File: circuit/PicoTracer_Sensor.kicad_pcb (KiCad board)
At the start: 2 copper layers, 150 x 46 mm, 19 parts, among them J8 Conn_01x08_Socket, U1 LBR-127HLD, U10 LBR-127HLD, U11 LBR-127HLD, U12 LBR-127HLD, U13 LBR-127HLD, U14 LBR-127HLD

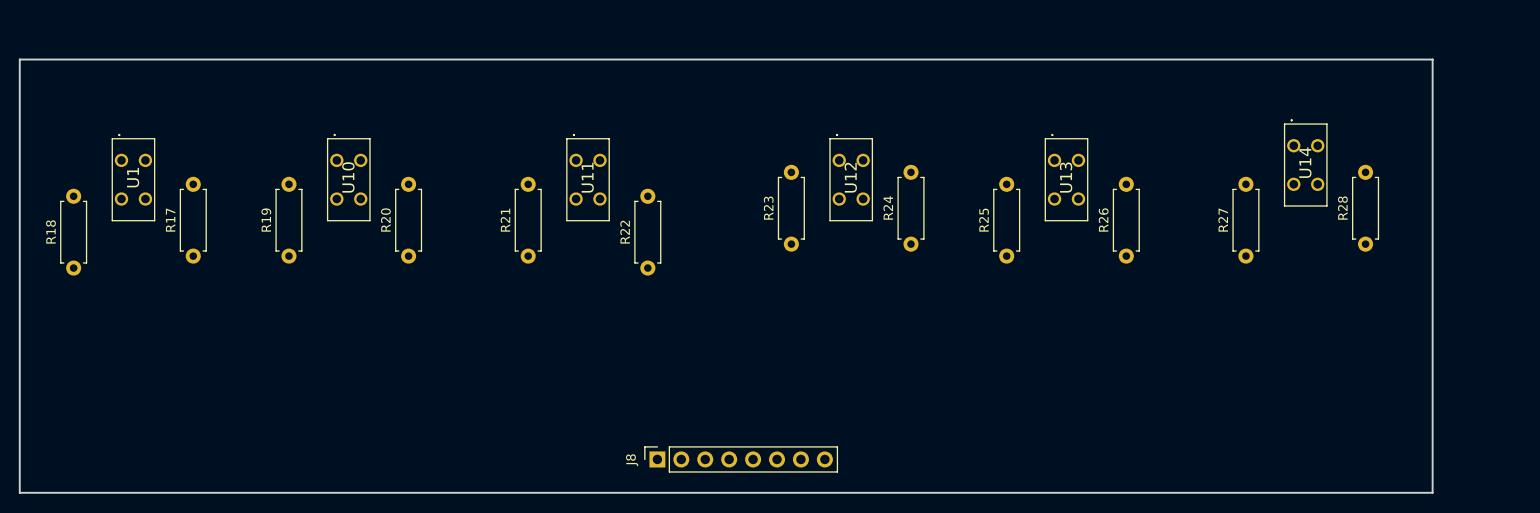
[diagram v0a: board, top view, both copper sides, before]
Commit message: 配線図：配線まで完了　ガーバーファイル出すときに水色の線を出さないよう注意！
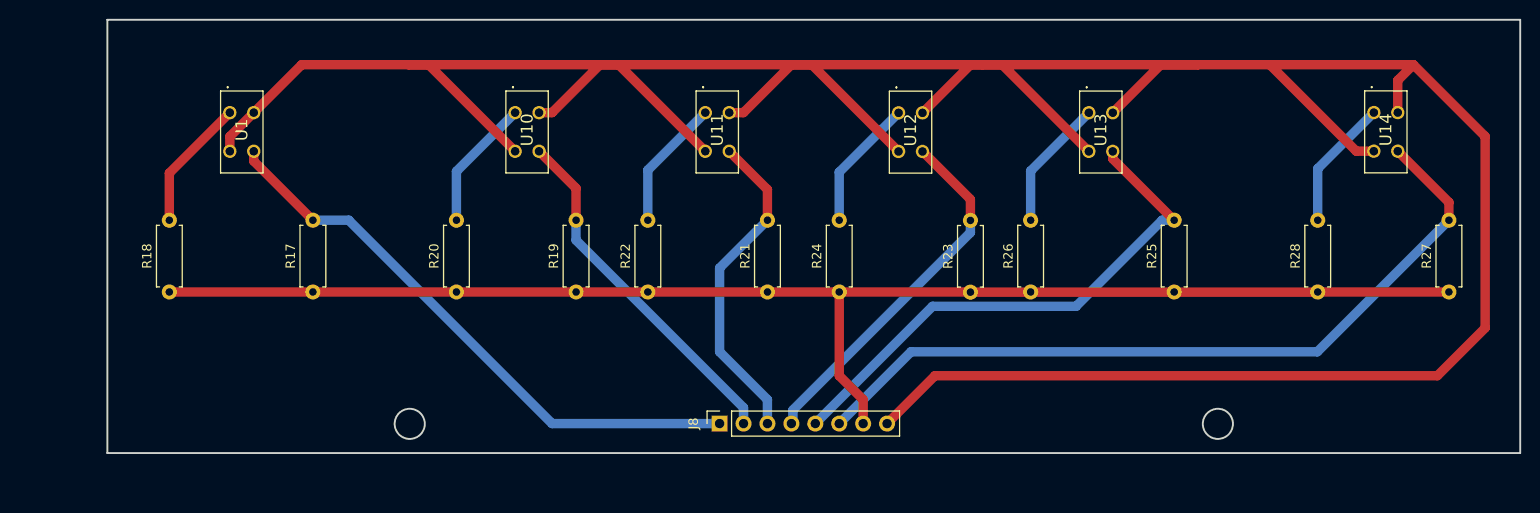
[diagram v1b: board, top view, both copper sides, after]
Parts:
- moved R19 30.7 mm to (121.9, 100.3)
- moved R21 25.7 mm to (142.2, 100.3)
- moved R27 21.9 mm to (214.6, 100.3)
- moved R23 19.7 mm to (163.8, 100.3)
- moved U10 19.6 mm to (115.5, 81.3)
- moved R25 18.2 mm to (185.4, 100.3)
- moved U11 14.6 mm to (135.6, 81.3)
- moved R17 13.3 mm to (94.0, 100.3)
- moved U1 12.6 mm to (85.2, 81.3)
- moved R26 10.9 mm to (170.2, 100.3)
- moved R18 10.5 mm to (78.7, 100.3)
- moved U14 9.20 mm to (206.6, 81.3)
- moved R24 9.16 mm to (149.9, 100.3)
- moved U12 8.07 mm to (156.2, 81.3)
- moved J8 7.62 mm to (137.2, 114.3)
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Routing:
- net Net-(J8-Pin_8): track 0.00 -> 347.1 mm
- net Net-(J8-Pin_7): track 0.00 -> 150.9 mm
- net Net-(J8-Pin_6): track 0.00 -> 83.3 mm
- net Net-(J8-Pin_1): track 0.00 -> 62.0 mm
- net Net-(J8-Pin_5): track 0.00 -> 57.1 mm
- net Net-(J8-Pin_4): track 0.00 -> 38.9 mm
- net Net-(J8-Pin_2): track 0.00 -> 37.9 mm
- net Net-(J8-Pin_3): track 0.00 -> 34.8 mm
- net Net-(U1-ANODE(LONG)): track 0.00 -> 14.1 mm
- net Net-(U12-ANODE(LONG)): track 0.00 -> 14.0 mm
- net Net-(U10-ANODE(LONG)): track 0.00 -> 14.0 mm
- net Net-(U13-ANODE(LONG)): track 0.00 -> 14.0 mm
- net Net-(U11-ANODE(LONG)): track 0.00 -> 13.9 mm
- net Net-(U14-ANODE(LONG)): track 0.00 -> 13.9 mm
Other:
- outline, holes or cut-outs redrawn

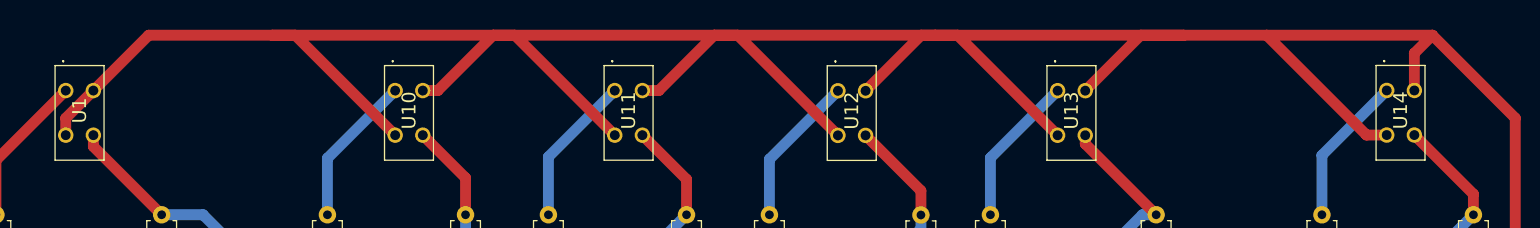
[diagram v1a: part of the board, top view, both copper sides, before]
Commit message: PicoTracer-backupsファイルを管理外に変更　センサー、メイン配線図ファイル修正、その他ファイル更新
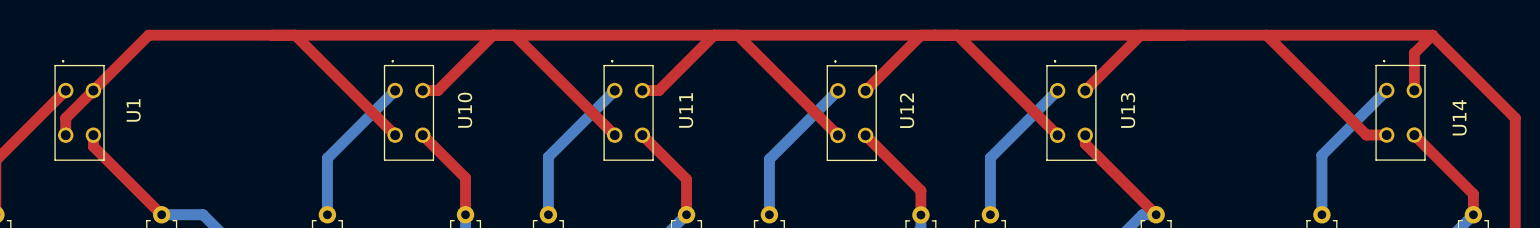
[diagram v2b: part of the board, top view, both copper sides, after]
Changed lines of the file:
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@@
 			(drillshape 0)
 			(scaleselection 1)
-			(outputdirectory "./")
+			(outputdirectory "PicoTracer_Sensor_Garber/")
 		)
 	)
@@
 		(tags "Undefined or Miscellaneous")
 		(property "Reference" "U13"
-			(at -1.825 1.27 90)
+			(at -1.825 6.52 90)
 			(layer "F.SilkS")
 			(effects
@@
 		)
 		(fp_text user "${REFERENCE}"
-			(at -1.825 1.27 90)
+			(at -1.825 6.52 90)
 			(layer "F.Fab")
 			(effects
@@
 		(tags "Undefined or Miscellaneous")
 		(property "Reference" "U10"
-			(at -1.825 1.27 90)
+			(at -1.825 6.47 90)
 			(layer "F.SilkS")
 			(effects
@@
 		)
 		(fp_text user "${REFERENCE}"
-			(at -1.825 1.27 90)
+			(at -1.825 6.47 90)
 			(layer "F.Fab")
 			(effects
@@
 		(tags "Undefined or Miscellaneous")
 		(property "Reference" "U11"
-			(at -1.825 1.27 90)
+			(at -1.825 6.6 90)
 			(layer "F.SilkS")
 			(effects
@@
 		)
 		(fp_text user "${REFERENCE}"
-			(at -1.825 1.27 90)
+			(at -1.825 6.6 90)
 			(layer "F.Fab")
 			(effects
@@
 		(tags "Undefined or Miscellaneous")
 		(property "Reference" "U12"
-			(at -1.825 1.27 90)
+			(at -1.825 6.4 90)
 			(layer "F.SilkS")
 			(effects
@@
 		)
 		(fp_text user "${REFERENCE}"
-			(at -1.825 1.27 90)
+			(at -1.825 6.4 90)
 			(layer "F.Fab")
 			(effects
@@
 		(tags "Undefined or Miscellaneous")
 		(property "Reference" "U1"
-			(at -1.825 1.27 90)
+			(at -1.825 6.28 90)
 			(layer "F.SilkS")
 			(effects
@@
 		(tags "Undefined or Miscellaneous")
 		(property "Reference" "U14"
-			(at -1.825 1.27 90)
+			(at -2.54 6.74 90)
 			(layer "F.SilkS")
 			(effects
@@
 		)
 		(fp_text user "${REFERENCE}"
-			(at -1.825 1.27 90)
+			(at -2.54 6.74 90)
 			(layer "F.Fab")
 			(effects
